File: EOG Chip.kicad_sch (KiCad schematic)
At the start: 15 parts, among them U1 INA128, U2 INA128, U3 TL074

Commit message: Added microcontroller and antenna
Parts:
- added AE1: Antenna, symbol Device:Antenna
- added FL1: MLPF-WB55-01E3, BUMPLESS_CSP_2025, symbol MLPF-WB55-01E3:MLPF-WB55-01E3
- added U4: STM32WB55CCUx, Package_DFN_QFN:QFN-48-1EP_7x7mm_P0.5mm_EP5.6x5.6mm, symbol MCU_ST_STM32WB:STM32WB55CCUx
- added Y1: Crystal, symbol Device:Crystal
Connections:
- net +5V: no longer R6.1
- net GND: no longer R5.2
- net HOR_OUT: now also U4.10 (PA1)
- net VERT_OUT: now also U4.9 (PA0)
- new net: AE1.1 (A), FL1.A1 (OUT)
- new net: FL1.A3 (IN), U4.21 (RF1)
- new net: U4.24 (OSC_OUT), Y1.2
- new net: U4.25 (OSC_IN), Y1.1
- new net +3V: R6.1, U4.1 (VBAT), U4.20 (VDD), U4.23 (VDDRF), U4.34 (VDDSMPS), U4.35 (VDD), U4.40 (VDDUSB), U4.48 (VDD), U4.8 (VDDA)
- new net GROUND: FL1.A2 (GND4), FL1.B1 (GND3), FL1.B2 (GND2), FL1.B3 (GND1), R5.2, U4.22 (VSSRF), U4.32 (VSSSMPS), U4.49 (VSS)

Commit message: updated files
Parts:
- AE1: footprint (none) -> antenna_ghz:ANTC3216X60N
- FL1: footprint BUMPLESS_CSP_2025 -> a_rf_module:BUMPLESS_CSP_2025
- Y1: footprint (none) -> new_crystal:ABM11A32000MHZD2YT3
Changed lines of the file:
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@@
 			)
 		)
-		(property "Footprint" ""
+		(property "Footprint" "antenna_ghz:ANTC3216X60N"
 			(at 287.02 52.07 0)
 			(effects
@@
 			)
 		)
-		(property "Footprint" ""
+		(property "Footprint" "new_crystal:ABM11A32000MHZD2YT3"
 			(at 274.32 55.88 0)
 			(effects
@@
 			)
 		)
-		(property "Footprint" "BUMPLESS_CSP_2025"
+		(property "Footprint" "a_rf_module:BUMPLESS_CSP_2025"
 			(at 311.15 59.69 0)
 			(effects

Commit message: updating schematics
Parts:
- U1, U2: footprint Package_DIP:DIP-8_W7.62mm -> amp_new:SOP65P490X110-8N
- U3: footprint Package_DIP:DIP-14_W7.62mm -> amp_new_big:SOIC127P600X175-14N
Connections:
- net REF_IN: now also U3.10 (+), U3.12 (+); no longer U3.10 (+), U3.12 (+)
- net at U2.5 (Ref), U3.5 (+): now also U3.8, U3.9 (-); no longer U3.13 (-), U3.14
- net at U1.5 (Ref), U3.3 (+): now also U3.13 (-), U3.14; no longer U3.8, U3.9 (-)
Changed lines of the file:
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@@
 			)
 		)
-		(property "Footprint" "Package_DIP:DIP-14_W7.62mm"
+		(property "Footprint" "amp_new_big:SOIC127P600X175-14N"
 			(at 124.46 88.9 0)
 			(effects
@@
 		(lib_id "Amplifier_Operational:TL074")
 		(at 156.21 91.44 0)
-		(unit 4)
+		(unit 3)
 		(exclude_from_sim no)
 		(in_bom yes)
@@
 			)
 		)
-		(property "Footprint" "Package_DIP:DIP-14_W7.62mm"
+		(property "Footprint" "amp_new_big:SOIC127P600X175-14N"
 			(at 154.94 88.9 0)
 			(effects
@@
 				(path "/3b24f0de-bb9a-4c55-8f2f-94868eba9d38"
 					(reference "U3")
-					(unit 4)
+					(unit 3)
 				)
 			)
@@
 			)
 		)
-		(property "Footprint" "Package_DIP:DIP-8_W7.62mm"
+		(property "Footprint" "amp_new:SOP65P490X110-8N"
 			(at 76.2 91.44 0)
 			(effects
@@
 			)
 		)
-		(property "Footprint" "Package_DIP:DIP-8_W7.62mm"
+		(property "Footprint" "amp_new:SOP65P490X110-8N"
 			(at 76.2 48.26 0)
 			(effects
@@
 			)
 		)
-		(property "Footprint" "Package_DIP:DIP-14_W7.62mm"
+		(property "Footprint" "amp_new_big:SOIC127P600X175-14N"
 			(at 124.46 45.72 0)
 			(effects
@@
 		(lib_id "Amplifier_Operational:TL074")
 		(at 156.21 48.26 0)
-		(unit 3)
+		(unit 4)
 		(exclude_from_sim no)
 		(in_bom yes)
@@
 			)
 		)
-		(property "Footprint" "Package_DIP:DIP-14_W7.62mm"
+		(property "Footprint" "amp_new_big:SOIC127P600X175-14N"
 			(at 154.94 45.72 0)
 			(effects
@@
 				(path "/3b24f0de-bb9a-4c55-8f2f-94868eba9d38"
 					(reference "U3")
-					(unit 3)
-				)
-			)
+					(unit 4)
+				)
+			)

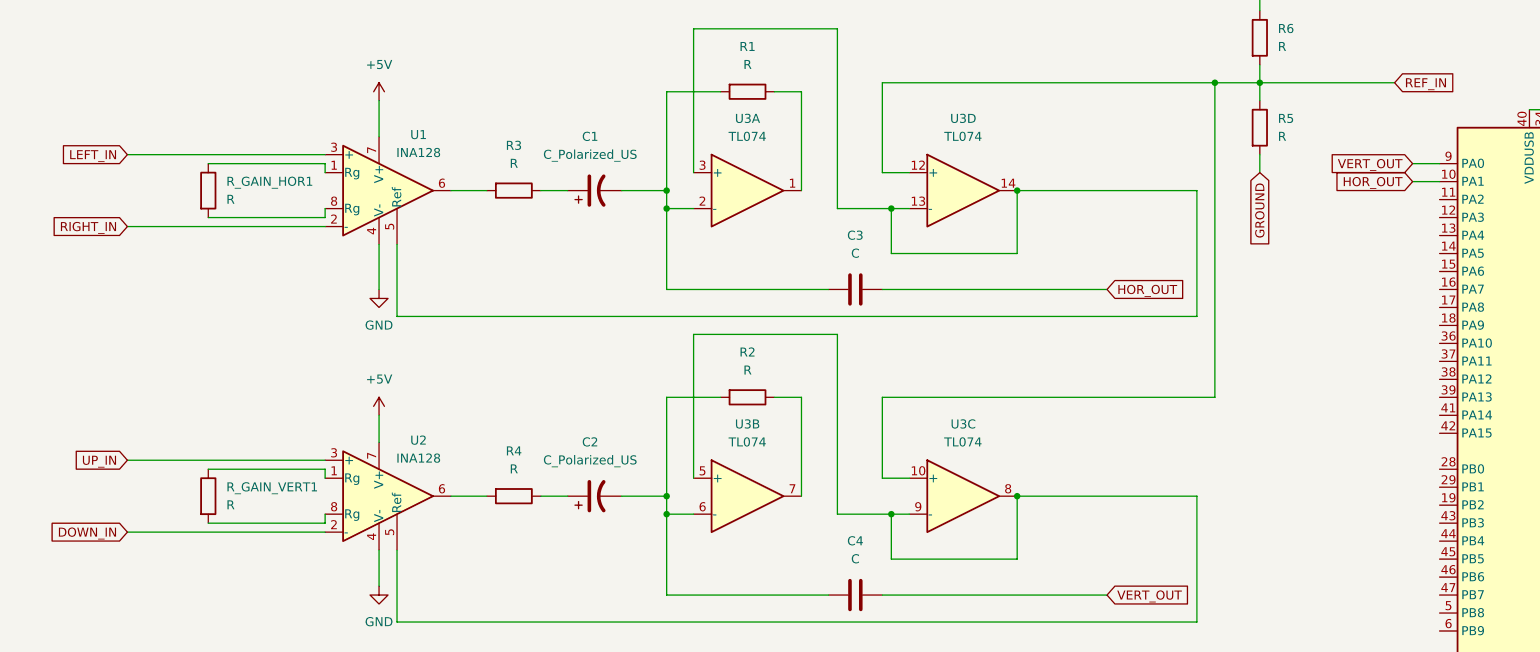
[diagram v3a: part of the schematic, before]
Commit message: Added potentiometers and started on traces
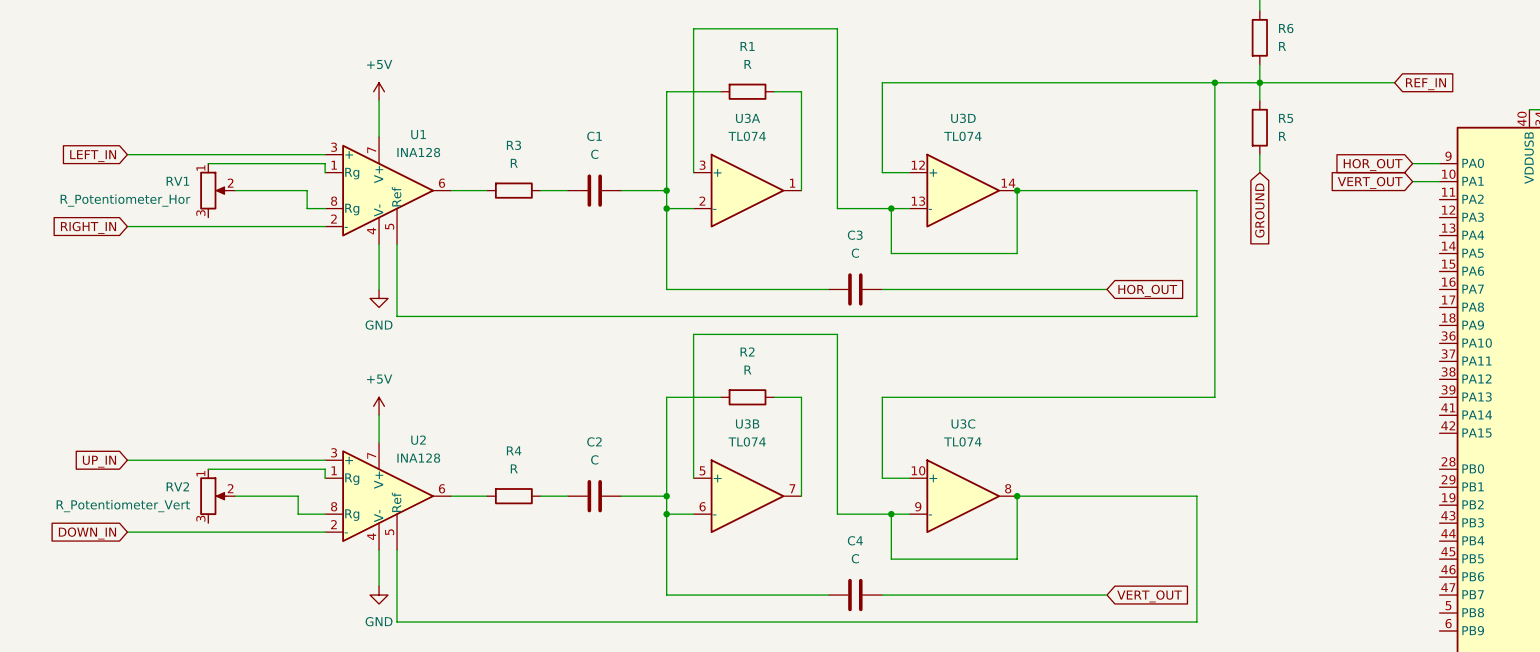
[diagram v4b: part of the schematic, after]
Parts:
- C1, C2: value C_Polarized_US -> C; footprint Capacitor_SMD:CP_Elec_5x4.5 -> Capacitor_SMD:C_0603_1608Metric; symbol Device:C_Polarized_US -> Device:C
- RV1: renamed from R_GAIN_HOR1; value R -> R_Potentiometer_Hor; footprint Resistor_SMD:R_0603_1608Metric -> Potentiometer_TSM:TSM41YJ503KR05; symbol Device:R -> Device:R_Potentiometer
- RV2: renamed from R_GAIN_VERT1; value R -> R_Potentiometer_Vert; footprint Resistor_SMD:R_0603_1608Metric -> Potentiometer_TSM:TSM41YJ503KR05; symbol Device:R -> Device:R_Potentiometer
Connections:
- net HOR_OUT: now also U4.9 (PA0); no longer U4.10 (PA1)
- net VERT_OUT: now also U4.10 (PA1); no longer U4.9 (PA0)
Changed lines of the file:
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@@
+	(wire
+		(pts
+			(xy 63.5 48.26) (xy 63.5 50.8)
+		)
+		(stroke
+			(width 0)
+			(type default)
+		)
+	)
 	(wire
 		(pts
@@
 	(wire
 		(pts
-			(xy 49.53 52.07) (xy 66.04 52.07)
-		)
-		(stroke
-			(width 0)
-			(type default)
-		)
-	)
-	(wire
-		(pts
 			(xy 114.3 93.98) (xy 114.3 91.44)
 		)
@@
 	(wire
 		(pts
+			(xy 53.34 91.44) (xy 62.23 91.44)
+		)
+		(stroke
+			(width 0)
+			(type default)
+		)
+	)
+	(wire
+		(pts
 			(xy 148.59 88.9) (xy 144.78 88.9)
 		)
@@
 	(wire
 		(pts
+			(xy 53.34 48.26) (xy 63.5 48.26)
+		)
+		(stroke
+			(width 0)
+			(type default)
+		)
+	)
+	(wire
+		(pts
 			(xy 138.43 25.4) (xy 138.43 50.8)
 		)
@@
 	(wire
 		(pts
+			(xy 62.23 91.44) (xy 62.23 93.98)
+		)
+		(stroke
+			(width 0)
+			(type default)
+		)
+	)
+	(wire
+		(pts
 			(xy 314.96 64.77) (xy 314.96 67.31)
 		)
@@
 	(wire
 		(pts
-			(xy 66.04 52.07) (xy 66.04 50.8)
+			(xy 62.23 93.98) (xy 66.04 93.98)
 		)
 		(stroke
@@
 	(wire
 		(pts
-			(xy 66.04 95.25) (xy 66.04 93.98)
-		)
-		(stroke
-			(width 0)
-			(type default)
-		)
-	)
-	(wire
-		(pts
 			(xy 269.24 59.69) (xy 274.32 59.69)
 		)
@@
 	(wire
 		(pts
-			(xy 49.53 95.25) (xy 66.04 95.25)
-		)
-		(stroke
-			(width 0)
-			(type default)
-		)
-	)
-	(wire
-		(pts
 			(xy 133.35 34.29) (xy 133.35 48.26)
 		)
@@
 		(pts
 			(xy 198.12 33.02) (xy 198.12 35.56)
+		)
+		(stroke
+			(width 0)
+			(type default)
+		)
+	)
+	(wire
+		(pts
+			(xy 63.5 50.8) (xy 66.04 50.8)
 		)
 		(stroke
@@
 		)
 	)
-	(global_label "HOR_OUT"
+	(global_label "VERT_OUT"
 		(shape input)
 		(at 219.71 46.99 180)
@@
 		)
 		(property "Intersheetrefs" "${INTERSHEET_REFS}"
-			(at 208.1976 46.99 0)
+			(at 207.6534 46.99 0)
 			(effects
 				(font
@@
 		)
 	)
-	(global_label "VERT_OUT"
+	(global_label "HOR_OUT"
 		(shape input)
 		(at 219.71 44.45 180)
@@
 		)
 		(property "Intersheetrefs" "${INTERSHEET_REFS}"
-			(at 207.6534 44.45 0)
+			(at 208.1976 44.45 0)
 			(effects
 				(font
@@
 	)
 	(symbol
-		(lib_id "Device:C_Polarized_US")
+		(lib_id "Device:C")
 		(at 104.14 91.44 90)
 		(unit 1)
@@
 		(fields_autoplaced yes)
 		(property "Reference" "C2"
-			(at 103.505 83.82 90)
-			(effects
-				(font
-					(size 1.27 1.27)
-				)
-			)
-		)
-		(property "Value" "C_Polarized_US"
-			(at 103.505 86.36 90)
-			(effects
-				(font
-					(size 1.27 1.27)
-				)
-			)
-		)
-		(property "Footprint" "Capacitor_SMD:CP_Elec_5x4.5"
-			(at 104.14 91.44 0)
+			(at 104.14 83.82 90)
+			(effects
+				(font
+					(size 1.27 1.27)
+				)
+			)
+		)
+		(property "Value" "C"
+			(at 104.14 86.36 90)
+			(effects
+				(font
+					(size 1.27 1.27)
+				)
+			)
+		)
+		(property "Footprint" "Capacitor_SMD:C_0603_1608Metric"
+			(at 107.95 90.4748 0)
 			(effects
 				(font
@@
 			)
 		)
-		(property "Description" "Polarized capacitor, US symbol"
+		(property "Description" "Unpolarized capacitor"
 			(at 104.14 91.44 0)
 			(effects
@@
 	)
 	(symbol
-		(lib_id "Device:R")
+		(lib_id "Device:R_Potentiometer")
 		(at 49.53 48.26 0)
 		(unit 1)
@@
 		(dnp no)
 		(fields_autoplaced yes)
-		(property "Reference" "R_GAIN_HOR1"
-			(at 52.07 46.9899 0)
-			(effects
-				(font
-					(size 1.27 1.27)
-				)
-				(justify left)
-			)
-		)
-		(property "Value" "R"
-			(at 52.07 49.5299 0)
-			(effects
-				(font
-					(size 1.27 1.27)
-				)
-				(justify left)
-			)
-		)
-		(property "Footprint" "Resistor_SMD:R_0603_1608Metric"
-			(at 47.752 48.26 90)
+		(property "Reference" "RV1"
+			(at 46.99 46.9899 0)
+			(effects
+				(font
+					(size 1.27 1.27)
+				)
+				(justify right)
+			)
+		)
+		(property "Value" "R_Potentiometer_Hor"
+			(at 46.99 49.5299 0)
+			(effects
+				(font
+					(size 1.27 1.27)
+				)
+				(justify right)
+			)
+		)
+		(property "Footprint" "Potentiometer_TSM:TSM41YJ503KR05"
+			(at 49.53 48.26 0)
 			(effects
 				(font
@@
 			)
 		)
-		(property "Description" "Resistor"
+		(property "Description" "Potentiometer"
 			(at 49.53 48.26 0)
 			(effects
@@
 		)
 		(pin "2"
+		)
+		(pin "3"
 		)
 		(instances
 			(project ""
 				(path "/3b24f0de-bb9a-4c55-8f2f-94868eba9d38"
-					(reference "R_GAIN_HOR1")
+					(reference "RV1")
 					(unit 1)
 				)
@@
 	)
 	(symbol
-		(lib_id "Device:R")
+		(lib_id "Device:R_Potentiometer")
 		(at 49.53 91.44 0)
 		(unit 1)
@@
 		(dnp no)
 		(fields_autoplaced yes)
-		(property "Reference" "R_GAIN_VERT1"
-			(at 52.07 90.1699 0)
-			(effects
-				(font
-					(size 1.27 1.27)
-				)
-				(justify left)
-			)
-		)
-		(property "Value" "R"
-			(at 52.07 92.7099 0)
-			(effects
-				(font
-					(size 1.27 1.27)
-				)
-				(justify left)
-			)
-		)
-		(property "Footprint" "Resistor_SMD:R_0603_1608Metric"
-			(at 47.752 91.44 90)
+		(property "Reference" "RV2"
+			(at 46.99 90.1699 0)
+			(effects
+				(font
+					(size 1.27 1.27)
+				)
+				(justify right)
+			)
+		)
+		(property "Value" "R_Potentiometer_Vert"
+			(at 46.99 92.7099 0)
+			(effects
+				(font
+					(size 1.27 1.27)
+				)
+				(justify right)
+			)
+		)
+		(property "Footprint" "Potentiometer_TSM:TSM41YJ503KR05"
+			(at 49.53 91.44 0)
 			(effects
 				(font
@@
 			)
 		)
-		(property "Description" "Resistor"
+		(property "Description" "Potentiometer"
 			(at 49.53 91.44 0)
 			(effects
@@
 		)
 		(pin "2"
+		)
+		(pin "3"
 		)
 		(instances
 			(project "EOG Chip"
 				(path "/3b24f0de-bb9a-4c55-8f2f-94868eba9d38"
-					(reference "R_GAIN_VERT1")
+					(reference "RV2")
 					(unit 1)
 				)
@@
 	)
 	(symbol
-		(lib_id "Device:C_Polarized_US")
+		(lib_id "Device:C")
 		(at 104.14 48.26 90)
 		(unit 1)
@@
 		(fields_autoplaced yes)
 		(property "Reference" "C1"
-			(at 103.505 40.64 90)
-			(effects
-				(font
-					(size 1.27 1.27)
-				)
-			)
-		)
-		(property "Value" "C_Polarized_US"
-			(at 103.505 43.18 90)
-			(effects
-				(font
-					(size 1.27 1.27)
-				)
-			)
-		)
-		(property "Footprint" "Capacitor_SMD:CP_Elec_5x4.5"
-			(at 104.14 48.26 0)
+			(at 104.14 40.64 90)
+			(effects
+				(font
+					(size 1.27 1.27)
+				)
+			)
+		)
+		(property "Value" "C"
+			(at 104.14 43.18 90)
+			(effects
+				(font
+					(size 1.27 1.27)
+				)
+			)
+		)
+		(property "Footprint" "Capacitor_SMD:C_0603_1608Metric"
+			(at 107.95 47.2948 0)
 			(effects
 				(font
@@
 			)
 		)
-		(property "Description" "Polarized capacitor, US symbol"
+		(property "Description" "Unpolarized capacitor"
 			(at 104.14 48.26 0)
 			(effects

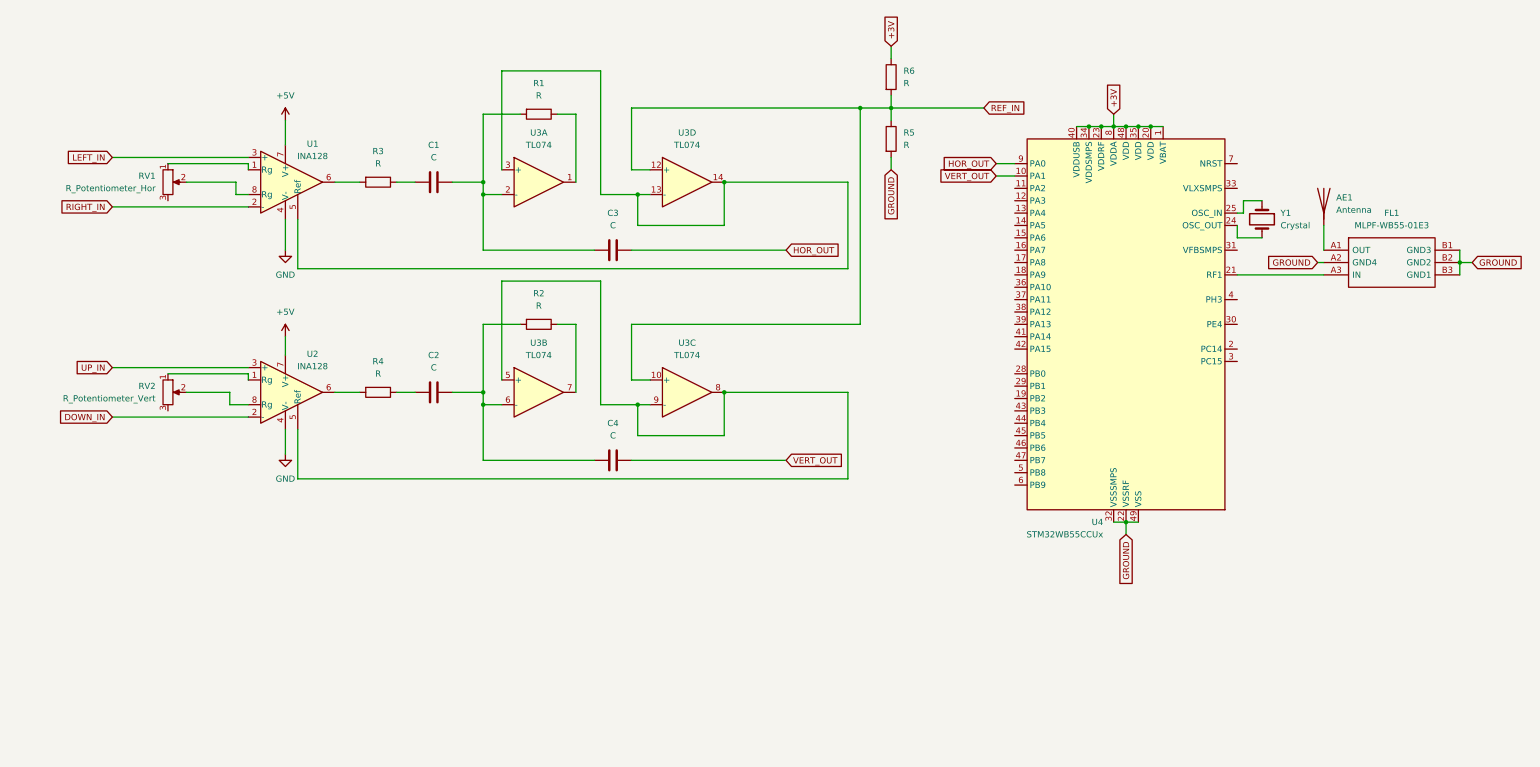
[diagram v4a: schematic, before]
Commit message: updated schematic and pcb
traces are almost finished
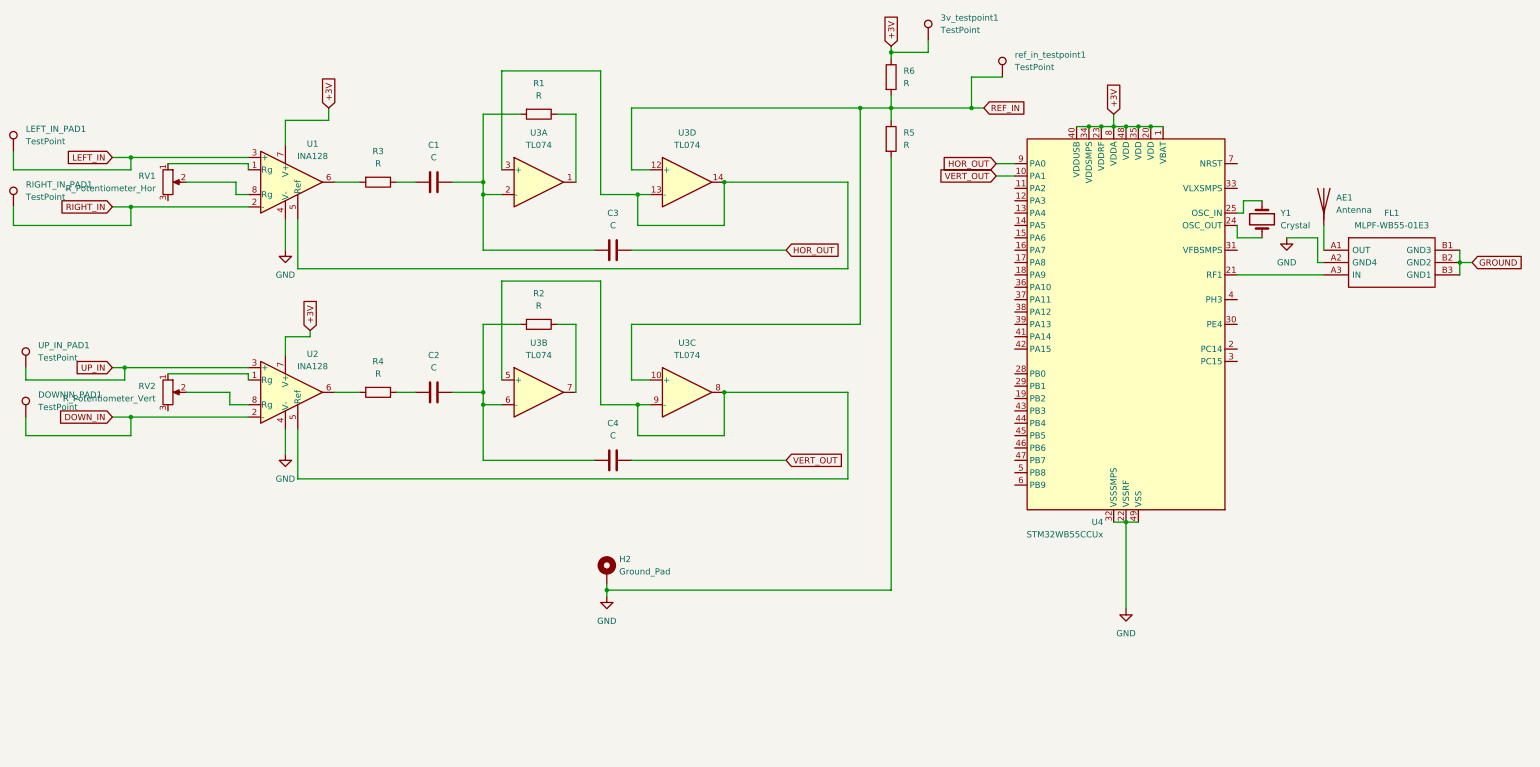
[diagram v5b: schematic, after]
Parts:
- added 3v_testpoint1, DOWNIN_PAD1, LEFT_IN_PAD1, RIGHT_IN_PAD1, UP_IN_PAD1, ref_in_testpoint1: TestPoint, TestPoint:TestPoint_Pad_1.0x1.0mm, symbol Connector:TestPoint
- added H2: Ground_Pad, MountingHole:MountingHole_2.2mm_M2_DIN965_Pad, symbol Mechanical:MountingHole_Pad
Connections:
- net +5V is gone; now on net +3V: U1.7 (V+), U2.7 (V+)
- net +3V: now also 3v_testpoint1.1
- net DOWN_IN: now also DOWNIN_PAD1.1
- net GND: now also FL1.A2 (GND4), R5.2, U4.22 (VSSRF), U4.32 (VSSSMPS), U4.49 (VSS), H2.1
- net GROUND: no longer FL1.A2 (GND4), R5.2, U4.22 (VSSRF), U4.32 (VSSSMPS), U4.49 (VSS)
- net LEFT_IN: now also LEFT_IN_PAD1.1
- net REF_IN: now also ref_in_testpoint1.1
- net RIGHT_IN: now also RIGHT_IN_PAD1.1
- net UP_IN: now also UP_IN_PAD1.1

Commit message: updated pcb and schematic
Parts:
- added H1, H3, H4, H5: MountingHole, MountingHole:MountingHole_2mm, symbol Mechanical:MountingHole
